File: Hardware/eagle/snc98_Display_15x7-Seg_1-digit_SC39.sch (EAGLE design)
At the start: 71 parts, among them M10 IRLML2244, M11 IRLML2244, M4 IRLML2244, M5 IRLML2244, M6 IRLML2244, M7 IRLML2244, M8 IRLML2244, M9 IRLML2244, X1 MICROMATCH-12, X2 MICROMATCH-14, X3 MICROMATCH-12, X4 MICROMATCH-14

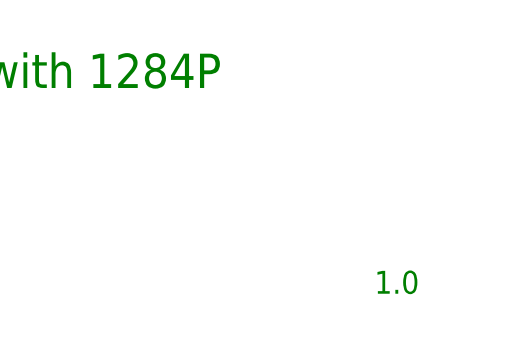
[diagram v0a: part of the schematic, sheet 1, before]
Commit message: Version 4 mechanical change
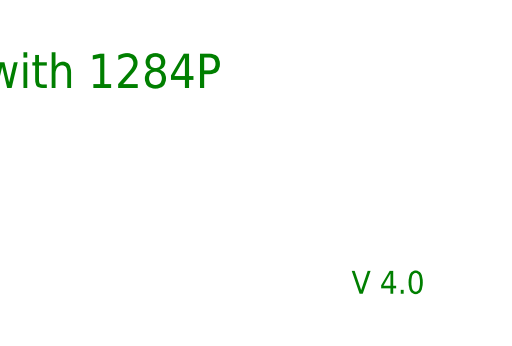
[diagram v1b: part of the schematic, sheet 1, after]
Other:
- note added: "V 4.0"
- note removed: "1.0"
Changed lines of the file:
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@@
 <text x="149.86" y="30.48" size="3.81" layer="91" ratio="12">Calculator 15-Digit with 1284P</text>
 <text x="149.86" y="25.4" size="2.54" layer="91" ratio="12">by Jens Grabner</text>
-<text x="238.76" y="7.62" size="2.54" layer="91" ratio="12">1.0</text>
+<text x="236.22" y="7.62" size="2.54" layer="91" ratio="12">V 4.0</text>
 <text x="5.08" y="10.16" size="2.1844" layer="91" ratio="10">Calculator 15-Digit with ATmega1284P by Jens Grabner is licensed under</text>
 <text x="5.08" y="15.24" size="3.81" layer="91" ratio="12">Copyright CERN 2013</text>
@@
 <text x="-58.42" y="58.42" size="3.81" layer="91" ratio="12">Calculator 15-Digit with 1284P</text>
 <text x="-58.42" y="53.34" size="2.54" layer="91" ratio="12">by Jens Grabner</text>
-<text x="30.48" y="35.56" size="2.54" layer="91" ratio="12">1.0</text>
+<text x="27.94" y="35.56" size="2.54" layer="91" ratio="12">V 4.0</text>
 <text x="-203.2" y="38.1" size="2.1844" layer="91" ratio="10">Calculator 15-Digit with ATmega1284P by Jens Grabner is licensed under</text>
 <text x="-203.2" y="43.18" size="3.81" layer="91" ratio="12">Copyright CERN 2013</text>
